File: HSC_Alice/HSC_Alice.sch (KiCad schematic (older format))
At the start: 231 parts, among them SW1 SW_Push, U1 ATmega32U4-AU, Y1 Crystal_GND24_Small

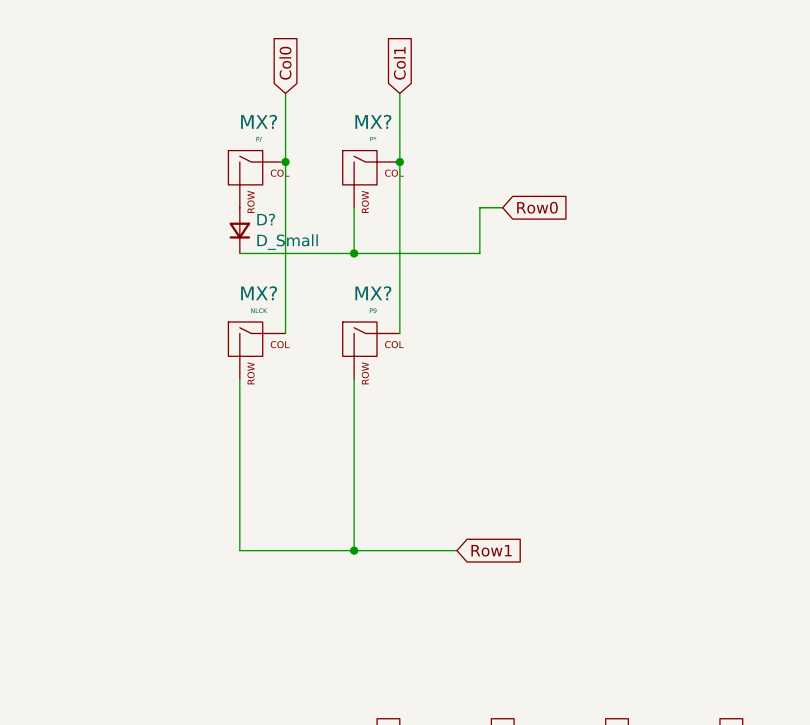
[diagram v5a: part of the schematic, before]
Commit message: Update PCB with Hot Swap sockets
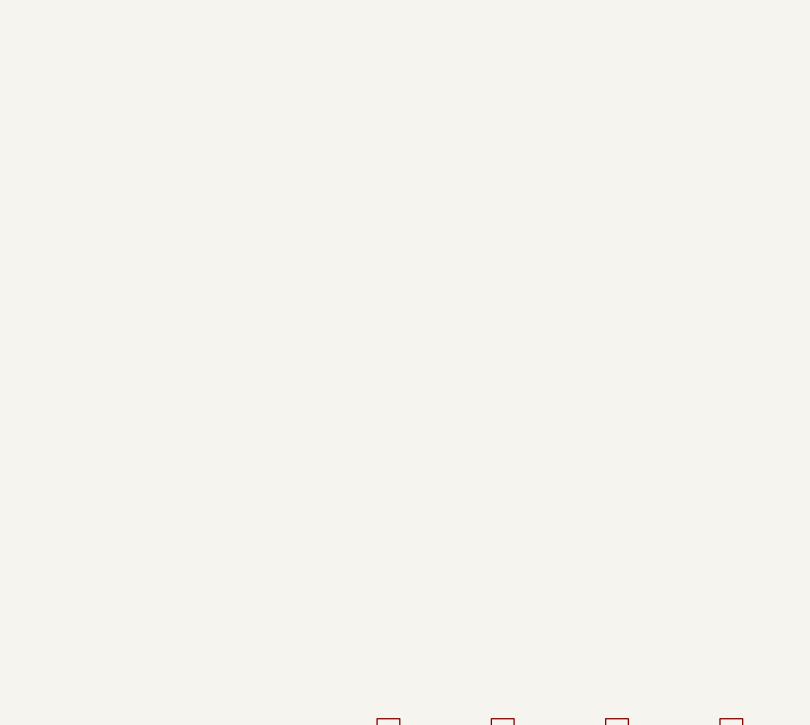
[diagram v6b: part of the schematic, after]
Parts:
- removed D?: D_Small, symbol Device:D_Small
- removed MX?: P/, MX_Alps_Hybrid:MX-1U-NoLED, symbol MX_Alps_Hybrid:MX-NoLED
- removed MX?: P*, MX_Alps_Hybrid:MX-1U-NoLED, symbol MX_Alps_Hybrid:MX-NoLED
- removed MX?: NLCK, MX_Alps_Hybrid:MX-1U-NoLED, symbol MX_Alps_Hybrid:MX-NoLED
- removed MX?: P9, MX_Alps_Hybrid:MX-1U-NoLED, symbol MX_Alps_Hybrid:MX-NoLED
- MX1, MX10, MX102, MX103, MX11, MX12, MX13, MX15, MX16, MX17, MX19, MX2, MX20, MX21, MX22, MX23, MX24, MX25, MX26, MX3, MX31, MX32, MX33, MX34, MX35, MX37, MX38, MX39, MX4, MX40, MX41, MX43, MX44, MX45, MX46, MX47, MX49, MX5, MX50, MX51, MX52, MX53, MX54, MX55, MX56, MX57, MX58, MX59, MX6, MX60, MX61, MX62, MX63, MX64, MX65, MX66, MX67, MX68, MX69, MX7, MX70, MX71, MX73, MX74, MX75, MX76, MX77, MX79, MX8, MX80, MX81, MX82, MX83, MX85, MX86, MX87, MX88, MX89, MX9, MX91, MX92, MX93, MX94, MX97, MX98, MX99: footprint MX_Alps_Hybrid:MX-1U-NoLED -> MX_Only:MXOnly-1U-Hotswap
- MX100: footprint MX_Alps_Hybrid:MX-2U-ReversedStabilizers-NoLED -> MX_Only:MXOnly-2U-Hotswap-ReversedStabilizers
- MX101, MX95: footprint MX_Alps_Hybrid:MX-2.25U-NoLED -> MX_Only:MXOnly-2.25U-Hotswap
- MX104, MX14, MX18: footprint MX_Alps_Hybrid:MX-2U-NoLED -> MX_Only:MXOnly-2U-Hotswap
- MX105, MX27: footprint MX_Alps_Hybrid:MX-1.5U-NoLED -> MX_Only:MXOnly-1.5U-Hotswap
- MX106, MX30, MX36, MX42, MX78, MX84, MX90, MX96: footprint MX_Alps_Hybrid:MX-1.25U-NoLED -> MX_Only:MXOnly-1.25U-Hotswap
- MX28: footprint MX_Alps_Hybrid:MX-1.75U-NoLED -> MX_Only:MXOnly-1.75U-Hotswap
- MX29: footprint MX_Alps_Hybrid:MX-1U-NoLED -> MX_Only:MXOnly-2.25U-Hotswap
- MX48, MX72: footprint MX_Alps_Hybrid:MX-2.75U-ReversedStabilizers-NoLED -> MX_Only:MXOnly-2.75U-Hotswap-ReversedStabilizers
